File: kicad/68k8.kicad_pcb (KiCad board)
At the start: 2 copper layers, 160 x 114.3 mm, 57 parts, among them J0 Barrel_Jack, J300 Conn_01x02_Male, J301 Conn_01x03_Male, J302 USB_B, J303 Conn_01x07, J320 Micro_SD_Card_Det, J330 Conn_02x04_Top_Bottom, SW110 SW_Push, U1 LF33_TO220, U100 68008D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

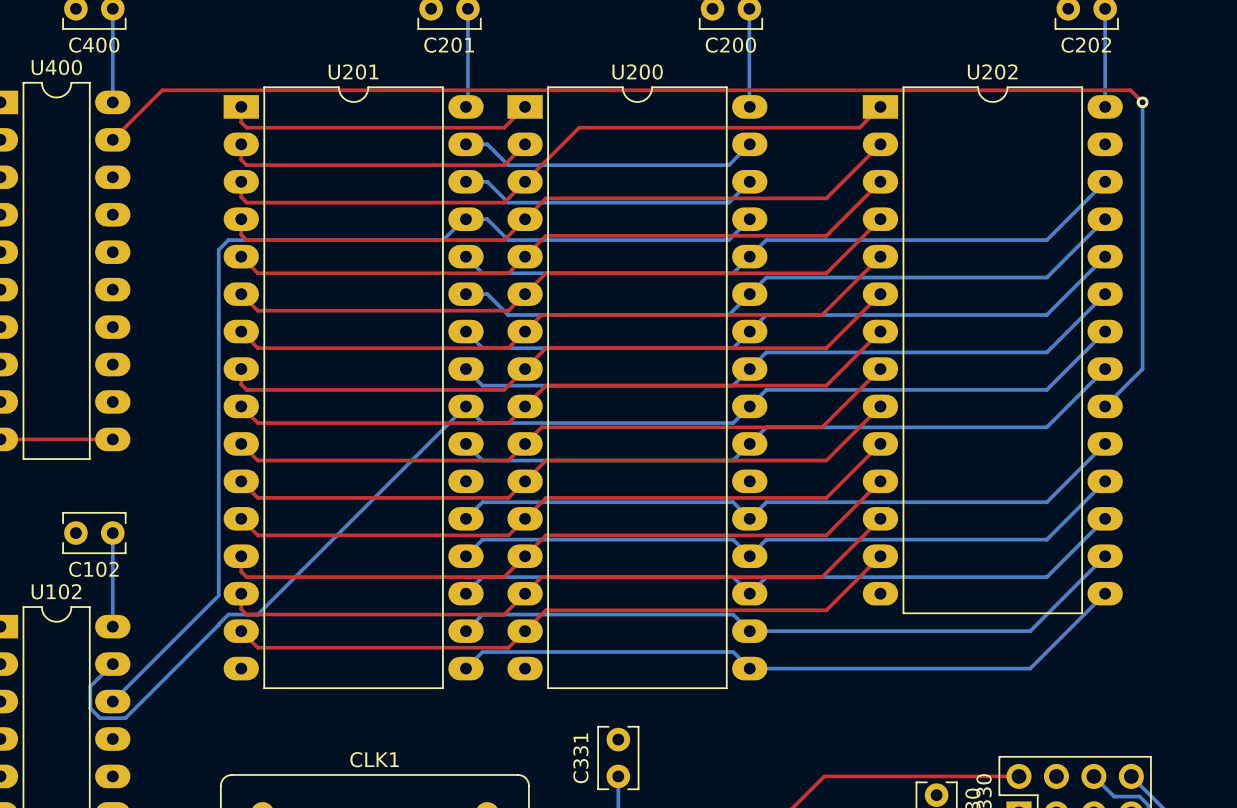
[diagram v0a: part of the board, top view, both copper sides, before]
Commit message: removed rom/ram routes
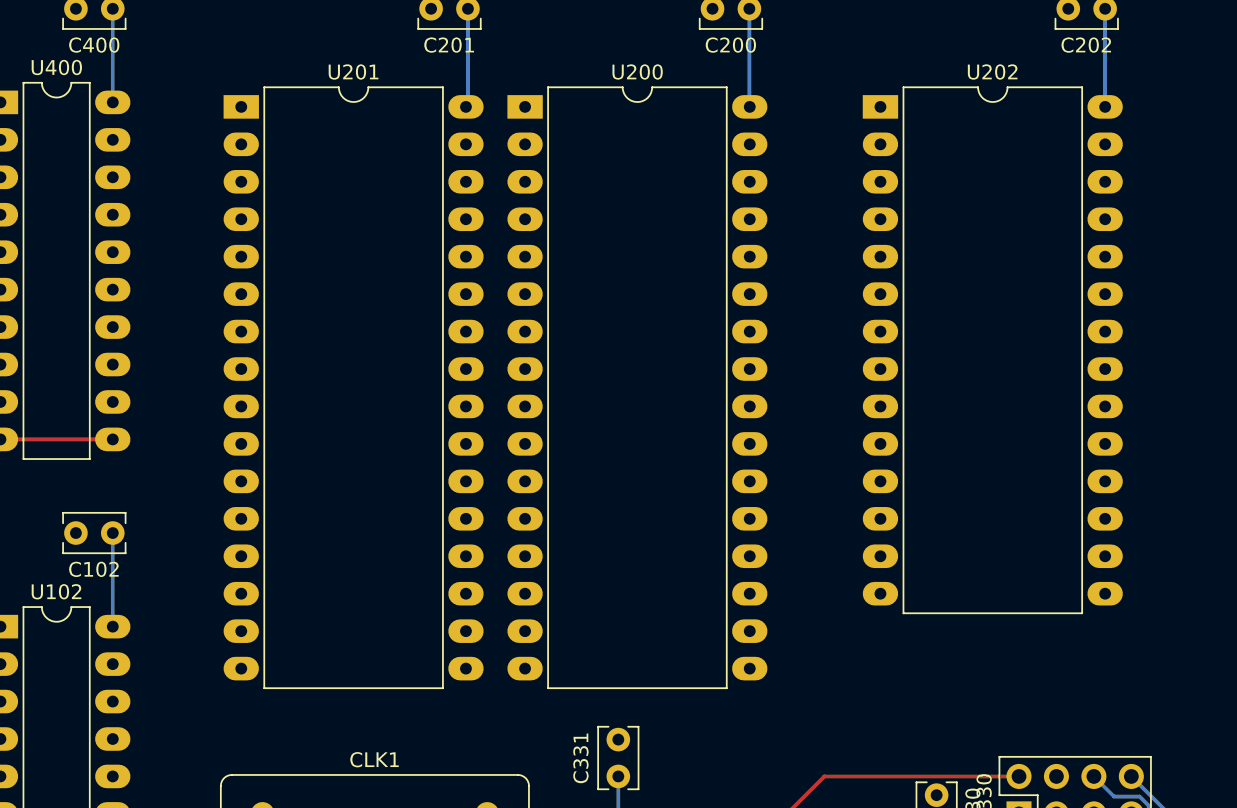
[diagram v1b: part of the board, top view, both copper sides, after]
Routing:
- net ROM_SEL: track 93.3 -> 0.00 mm, vias 1 -> 0
- net READ: track 84.6 -> 0.00 mm
- net WRITE: track 71.7 -> 0.00 mm
- net /100_CPU/D1: track 47.2 -> 0.00 mm
- net /100_CPU/D0: track 47.2 -> 0.00 mm
- net /100_CPU/A14: track 47.2 -> 0.00 mm
- net /100_CPU/A12: track 47.2 -> 0.00 mm
- net /100_CPU/A4: track 47.2 -> 0.00 mm
- net /100_CPU/A8: track 46.6 -> 0.00 mm
- net /100_CPU/A9: track 46.4 -> 0.00 mm
- net /100_CPU/A13: track 46.4 -> 0.00 mm
- net /100_CPU/D7: track 46.4 -> 0.00 mm
- net /100_CPU/D6: track 46.4 -> 0.00 mm
- net /100_CPU/D5: track 46.4 -> 0.00 mm
- net /100_CPU/D3: track 46.4 -> 0.00 mm
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
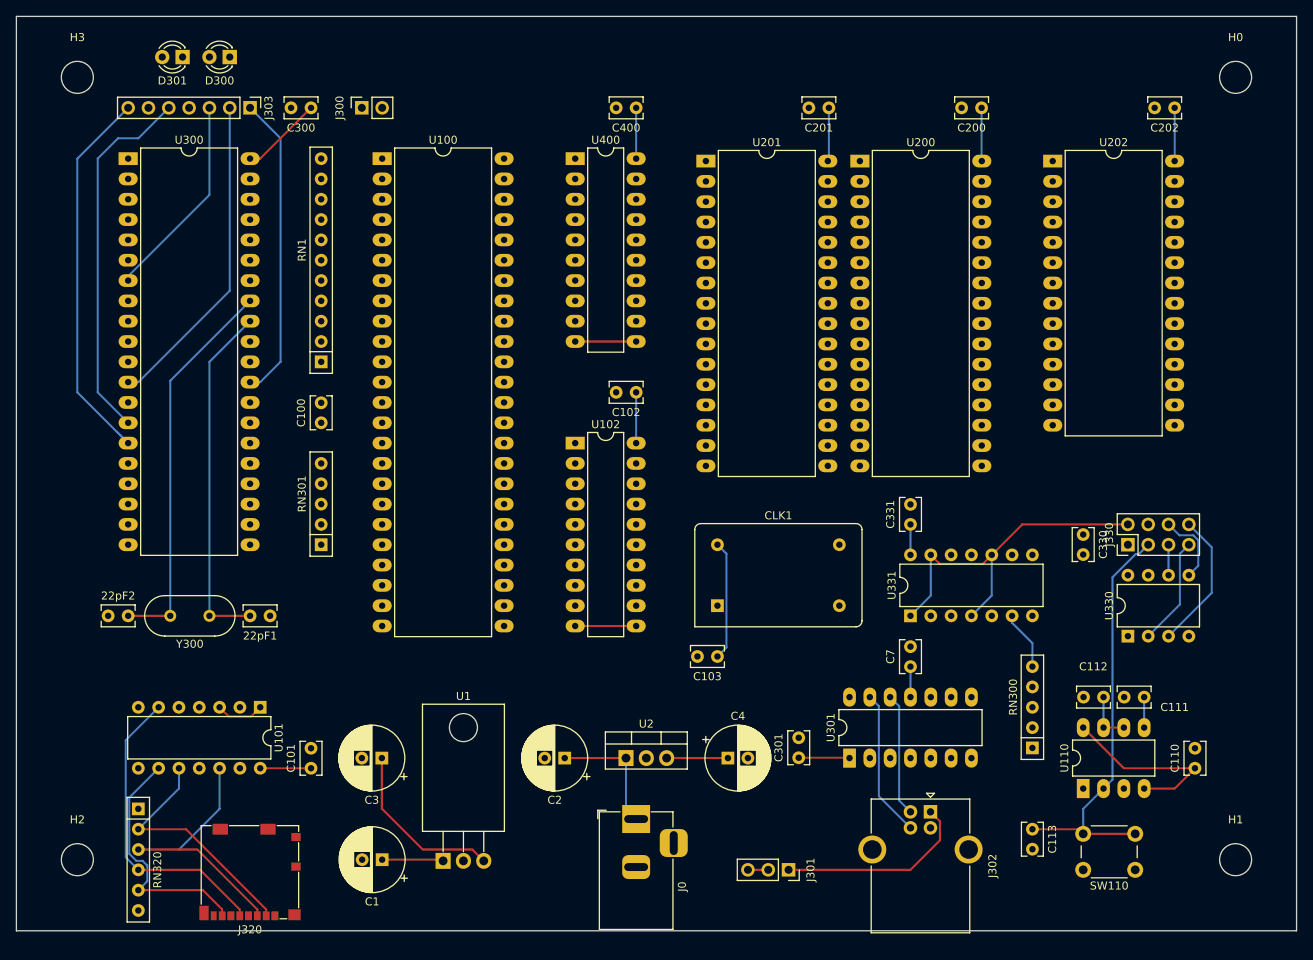
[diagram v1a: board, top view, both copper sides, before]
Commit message: moved larger footprints around a bit
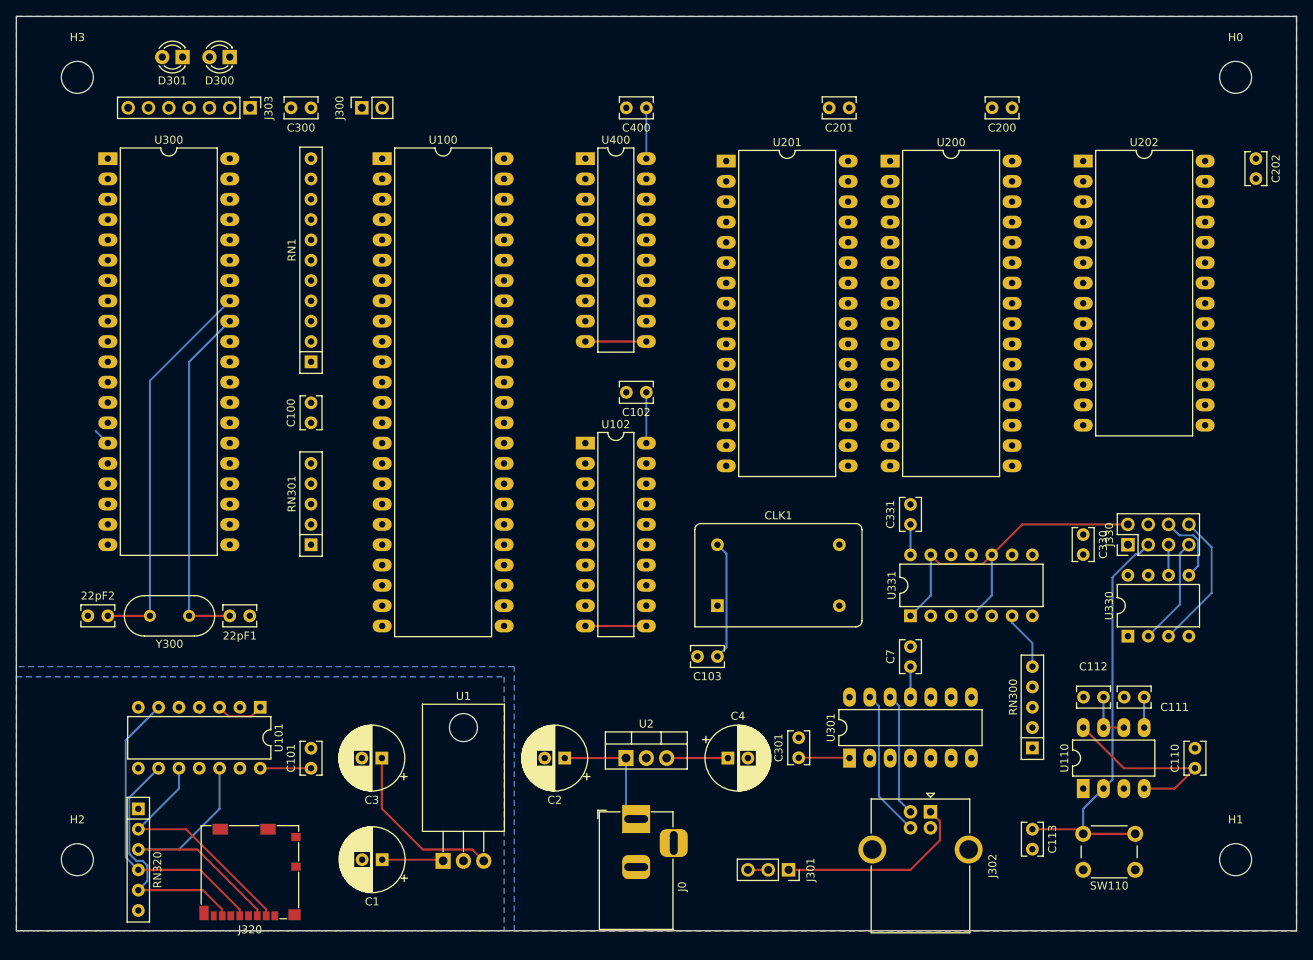
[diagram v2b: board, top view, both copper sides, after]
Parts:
- moved C202 12.0 mm to (287.0, 27.9), turned to 270 degrees
- moved C200 3.81 mm to (256.5, 21.6)
- moved U202 3.81 mm to (265.4, 28.2)
- moved U200 3.78 mm to (241.3, 28.2)
- moved 22pF2 2.54 mm to (141.0, 85.1)
- moved C201 2.54 mm to (236.2, 21.6)
- moved U300 2.54 mm to (143.5, 27.9)
- moved Y300 2.54 mm to (153.7, 85.1)
- moved 22pF1 2.54 mm to (161.2, 85.1)
- moved U201 2.54 mm to (220.8, 28.2)
- moved C100 1.27 mm to (168.9, 61.0)
- moved RN1 1.27 mm to (168.9, 53.3)
- moved RN301 1.27 mm to (168.9, 76.2)
- moved C102 1.27 mm to (210.8, 57.1)
- moved C400 1.27 mm to (210.8, 21.6)
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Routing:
- net AUX_CS4: track 49.7 -> 2.16 mm
- net AUX_CS2: track 46.1 -> 0.00 mm
- net MOSI: track 40.3 -> 0.00 mm
- net SCLK: track 38.2 -> 0.00 mm
- net +5V: track 105.5 -> 75.3 mm
- net MISO: track 33.2 -> 7.95 mm
- added copper zone on B.Cu, net +3V3
- added copper zone on B.Cu, net +5V
- added copper zone on F.Cu, net GND

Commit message: ran autoroute
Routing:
- net /100_CPU/A1: track 0.00 -> 243.2 mm, vias 0 -> 3
- net /100_CPU/A3: track 0.00 -> 222.3 mm, vias 0 -> 1
- net MISO: track 7.95 -> 218.2 mm
- net MOSI: track 0.00 -> 208.3 mm
- net /100_CPU/A13: track 0.00 -> 184.8 mm, vias 0 -> 1
- net SCLK: track 0.00 -> 184.0 mm
- net /100_CPU/D3: track 0.00 -> 168.9 mm
- net /100_CPU/D7: track 0.00 -> 168.8 mm, vias 0 -> 1
- net RESET_IN: track 52.8 -> 219.8 mm
- net +5V: track 75.3 -> 236.4 mm, vias 0 -> 16
- net /100_CPU/D5: track 0.00 -> 158.7 mm
- net /100_CPU/D0: track 0.00 -> 152.1 mm, vias 0 -> 2
- net /100_CPU/A4: track 0.00 -> 149.4 mm
- net /100_CPU/D6: track 0.00 -> 146.1 mm, vias 0 -> 1
- net /100_CPU/A2: track 0.00 -> 145.7 mm, vias 0 -> 1
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
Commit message: redid layout
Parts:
- RN320: value R_Network05 -> 10k
- moved J330 117.9 mm to (161.3, 119.4)
- moved U330 111.0 mm to (161.3, 104.1), turned to 0 degrees
- moved C330 98.4 mm to (168.9, 94.0), turned to 180 degrees
- moved U331 98.4 mm to (147.3, 104.1), turned to 0 degrees
- moved C331 86.2 mm to (160.0, 94.0), turned to 180 degrees
- moved RN300 83.9 mm to (175.3, 105.4), turned to 270 degrees
- moved J303 74.3 mm to (139.7, 92.7), turned to 0 degrees
- moved D301 72.3 mm to (139.7, 86.4), turned to 270 degrees
- moved C2 69.6 mm to (269.2, 91.4)
- moved D300 67.5 mm to (139.7, 80.0), turned to 270 degrees
- moved U2 61.0 mm to (269.2, 102.9)
- moved C4 59.5 mm to (279.4, 91.4)
- moved RN320 48.4 mm to (195.6, 105.4)
- moved J320 45.7 mm to (207.0, 116.8)
- moved C1 39.4 mm to (214.6, 101.6)
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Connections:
- J330 pad 2: PROG_EN -> PROG_SCLK
- J330 pad 4: +5V -> PROG_WP
- J330 pad 5: PROG_SCLK -> PROG_EN
- J330 pad 6: PROG_MOSI -> PROG_MISO
- J330 pad 7: PROG_MISO -> +5V
- J330 pad 8: PROG_WP -> PROG_MOSI
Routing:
- net /100_CPU/A1: track 243.2 -> 0.00 mm, vias 3 -> 0
- net +5V: track 236.4 -> 8.15 mm, vias 16 -> 0
- net /100_CPU/A3: track 222.3 -> 0.00 mm, vias 1 -> 0
- net MOSI: track 208.3 -> 0.00 mm
- net /100_CPU/A13: track 184.8 -> 0.00 mm, vias 1 -> 0
- net SCLK: track 184.0 -> 0.00 mm
- net RESET_IN: track 219.8 -> 37.9 mm
- net /100_CPU/D3: track 168.9 -> 0.00 mm
- net /100_CPU/D7: track 168.8 -> 0.00 mm, vias 1 -> 0
- net /100_CPU/D5: track 158.7 -> 0.00 mm
- net /100_CPU/D0: track 152.1 -> 0.00 mm, vias 2 -> 0
- net GND: track 151.5 -> 0.00 mm, vias 12 -> 0
- net /100_CPU/A4: track 149.4 -> 0.00 mm
- net /100_CPU/D6: track 146.1 -> 0.00 mm, vias 1 -> 0
- net /100_CPU/A2: track 145.7 -> 0.00 mm, vias 1 -> 0
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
